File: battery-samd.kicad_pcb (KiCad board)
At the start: 2 copper layers, 77.4 x 82.2 mm, 56 parts, among them J1 USB_B_Micro, J2 DebugEdge_02x03, J3 Conn_01x04_Male, Q1 BSS84, SW1 SW_Push, SW2 SW_SPDT, U1 AP2112K-3.3, U2 SAMD21E, U3 AT25SF081-SSHD-X

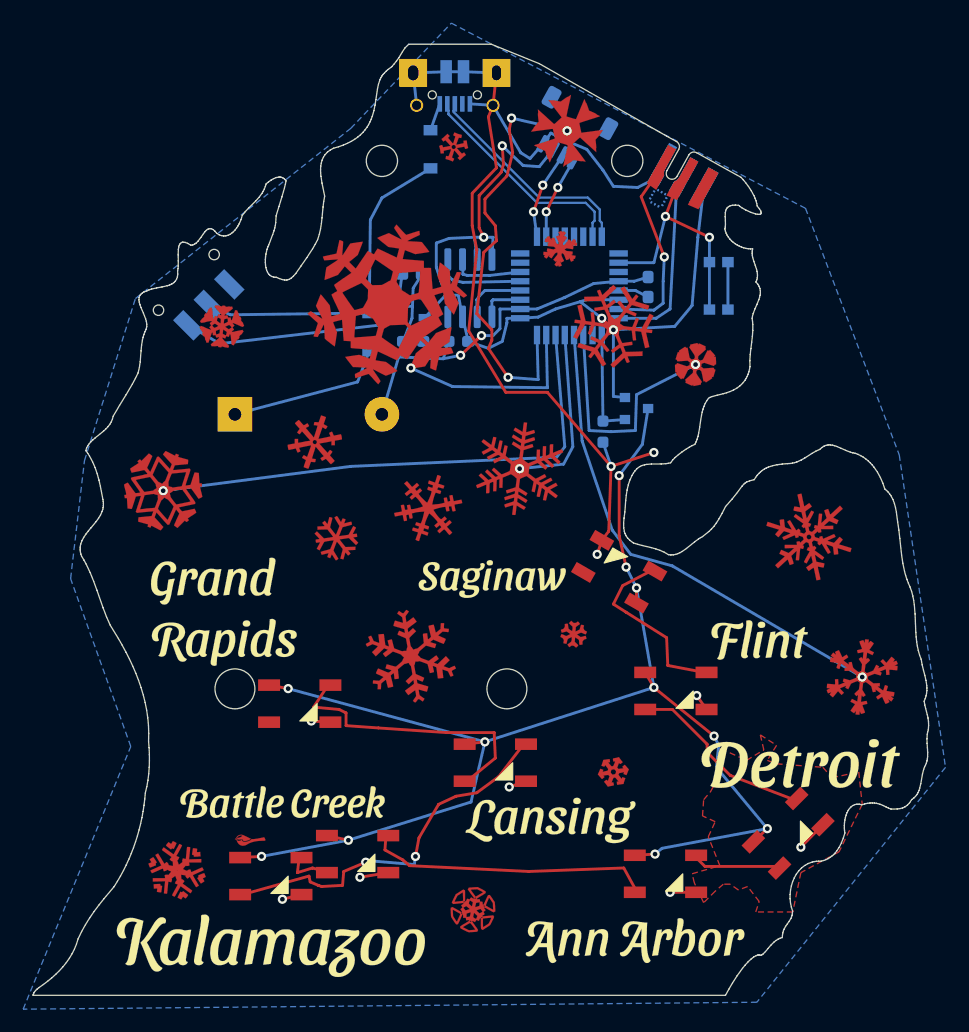
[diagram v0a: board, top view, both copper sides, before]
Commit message: Connect neopixel and add caps
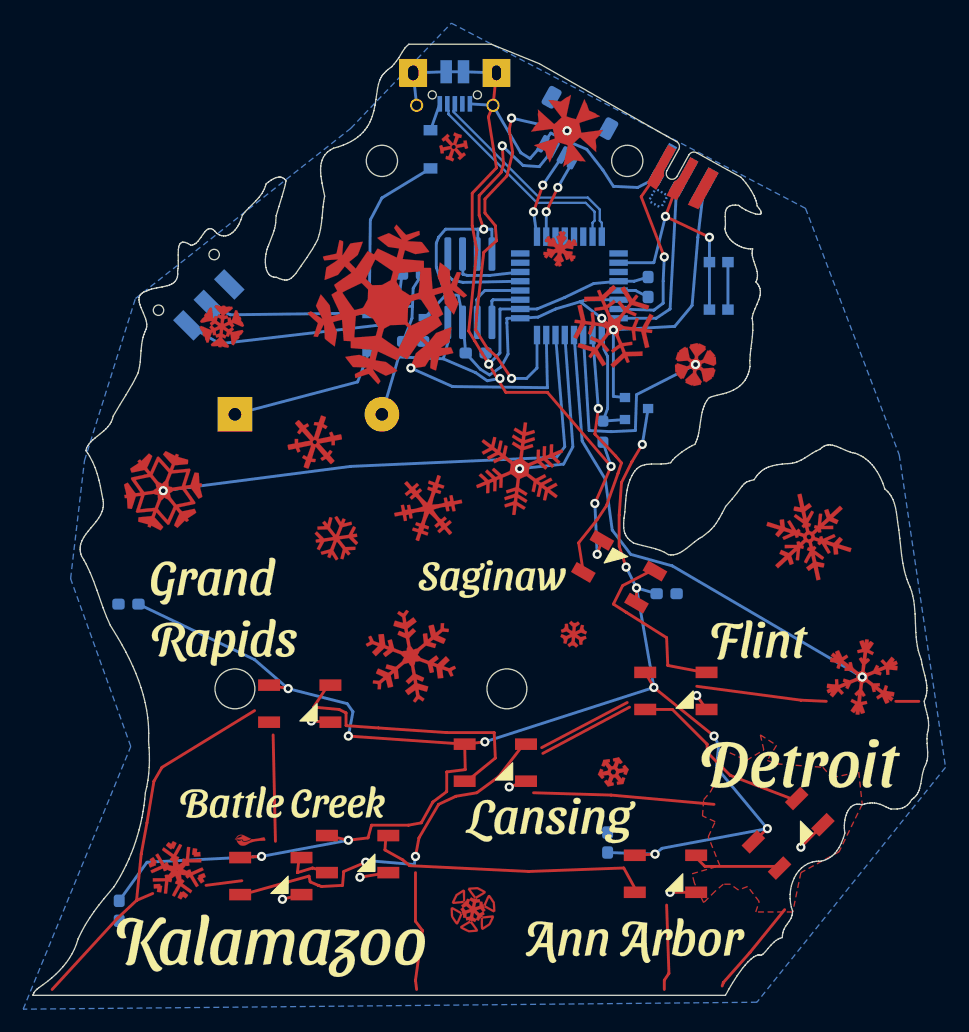
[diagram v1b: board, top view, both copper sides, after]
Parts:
- added C5: 1uF, Capacitor_SMD:C_0603_1608Metric_Pad1.08x0.95mm_HandSolder, B.Cu at (220.7, 129.0)
- added C6: 1uF, Capacitor_SMD:C_0603_1608Metric_Pad1.08x0.95mm_HandSolder, B.Cu at (225.8, 107.5)
- added C7: 1uF, Capacitor_SMD:C_0603_1608Metric_Pad1.08x0.95mm_HandSolder, B.Cu at (179.3, 108.4)
- added C8: 1uF, Capacitor_SMD:C_0603_1608Metric_Pad1.08x0.95mm_HandSolder, B.Cu at (178.5, 134.9)
- moved C4 1.80 mm to (209.3, 86.7), turned to 0 degrees
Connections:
- D3 pad 4: Net-(D3-Pad4) -> /NEOPIXEL
- U2 pad 2: Net-(U2-Pad2) -> /NEOPIXEL
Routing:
- net (no net): track 0.00 -> 93.6 mm
- net VCC: track 122.1 -> 157.3 mm, vias 11 -> 12
- net GND: track 148.3 -> 173.5 mm
- net /NEOPIXEL: track 0.00 -> 22.5 mm, vias 0 -> 1
- net +3V3: track 81.5 -> 86.8 mm
- net Net-(TP1-Pad1): track 36.6 -> 35.6 mm
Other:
- board text added: "ckd.tech/michigan/v2"
- board text removed: "ckd.tech/michigan/v1"
